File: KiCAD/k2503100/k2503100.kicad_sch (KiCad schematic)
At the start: 14 parts, among them J1 Power, J10 Analog, J11 Digital, J12 PWM, J13 PWM, J14 Communication, J2 PWM, J3 Analog, J4 PWM, J5 Analog, J6 Communication, J7 Digital, J8 Power, J9 Analog

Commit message: 途中
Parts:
- added J15: Power, Connector_PinSocket_2.54mm:PinSocket_1x08_P2.54mm_Vertical, symbol Connector_Generic:Conn_01x08
- added J16, J17: Analog, Connector_PinSocket_2.54mm:PinSocket_1x08_P2.54mm_Vertical, symbol Connector_Generic:Conn_01x08
- added J18: Digital, Connector_PinSocket_2.54mm:PinSocket_2x18_P2.54mm_Vertical, symbol Connector_Generic:Conn_02x18_Odd_Even
- added J19: PWM, Connector_PinSocket_2.54mm:PinSocket_1x10_P2.54mm_Vertical, symbol Connector_Generic:Conn_01x10
- added J20: PWM, Connector_PinSocket_2.54mm:PinSocket_1x08_P2.54mm_Vertical, symbol Connector_Generic:Conn_01x08
- added J21: Communication, Connector_PinSocket_2.54mm:PinSocket_1x08_P2.54mm_Vertical, symbol Connector_Generic:Conn_01x08
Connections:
- net *10: now also J19.8 (Pin_8)
- net *11: now also J19.7 (Pin_7)
- net *12: now also J19.6 (Pin_6)
- net *13: now also J19.5 (Pin_5)
- net *2: now also J20.6 (Pin_6)
- net *3: now also J20.5 (Pin_5)
- net *4: now also J20.4 (Pin_4)
- net *44: now also J18.11 (Pin_11)
- net *45: now also J18.12 (Pin_12)
- net *46: now also J18.9 (Pin_9)
- net *5: now also J20.3 (Pin_3)
- net *52: now also J18.3 (Pin_3)
- net *6: now also J20.2 (Pin_2)
- net *7: now also J20.1 (Pin_1)
- net *8: now also J19.10 (Pin_10)
- net *9: now also J19.9 (Pin_9)
- net +3V3: now also J15.4 (Pin_4)
- net +5V: now also J15.5 (Pin_5), J18.35 (Pin_35), J18.36 (Pin_36)
- net 22: now also J18.33 (Pin_33)
- net 23: now also J18.34 (Pin_34)
- net 24: now also J18.31 (Pin_31)
- net 25: now also J18.32 (Pin_32)
- net 26: now also J18.29 (Pin_29)
- net 27: now also J18.30 (Pin_30)
- net 28: now also J18.27 (Pin_27)
- net 29: now also J18.28 (Pin_28)
- net 30: now also J18.25 (Pin_25)
- net 31: now also J18.26 (Pin_26)
- net 32: now also J18.23 (Pin_23)
- net 33: now also J18.24 (Pin_24)
- net 34: now also J18.21 (Pin_21)
- net 35: now also J18.22 (Pin_22)
- net 36: now also J18.19 (Pin_19)
- net 37: now also J18.20 (Pin_20)
- net 38: now also J18.17 (Pin_17)
- net 39: now also J18.18 (Pin_18)
- net 40: now also J18.15 (Pin_15)
- net 41: now also J18.16 (Pin_16)
- net 42: now also J18.13 (Pin_13)
- net 43: now also J18.14 (Pin_14)
- net 47: now also J18.10 (Pin_10)
- net 48: now also J18.7 (Pin_7)
- net 49: now also J18.8 (Pin_8)
- net 50: now also J18.5 (Pin_5)
- net 51: now also J18.6 (Pin_6)
- net 53: now also J18.4 (Pin_4)
- net A0: now also J16.1 (Pin_1)
- net A1: now also J16.2 (Pin_2)
- net A10: now also J17.3 (Pin_3)
- net A11: now also J17.4 (Pin_4)
- net A12: now also J17.5 (Pin_5)
- net A13: now also J17.6 (Pin_6)
- net A14: now also J17.7 (Pin_7)
- net A15: now also J17.8 (Pin_8)
- net A2: now also J16.3 (Pin_3)
- net A3: now also J16.4 (Pin_4)
- net A4: now also J16.5 (Pin_5)
- net A5: now also J16.6 (Pin_6)
- net A6: now also J16.7 (Pin_7)
- net A7: now also J16.8 (Pin_8)
- net A8: now also J17.1 (Pin_1)
- net A9: now also J17.2 (Pin_2)
- net AREF: now also J19.3 (Pin_3)
- net GND: now also J15.6 (Pin_6), J15.7 (Pin_7), J18.1 (Pin_1), J18.2 (Pin_2), J19.4 (Pin_4)
- net IOREF: now also J15.2 (Pin_2)
- net RX0/0: now also J20.8 (Pin_8)
- net RX1/19: now also J21.6 (Pin_6)
- net RX2/17: now also J21.4 (Pin_4)
- net RX3/15: now also J21.2 (Pin_2)
- net SCL/21: now also J19.1 (Pin_1), J21.8 (Pin_8)
- net SDA/20: now also J19.2 (Pin_2), J21.7 (Pin_7)
- net TX0/1: now also J20.7 (Pin_7)
- net TX1/18: now also J21.5 (Pin_5)
- net TX2/16: now also J21.3 (Pin_3)
- net TX3/14: now also J21.1 (Pin_1)
- net VCC: now also J15.8 (Pin_8)
- net ~{RESET}: now also J15.3 (Pin_3)
- no-connect marks 2 -> 3
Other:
- added sheet Keyboard_Unit (Keyboard.kicad_sch)
- added sheet Relay_UNiT Sheet (Relay_Unit.kicad_sch)
- moved on the sheet: J1, J10, J11, J12, J13, J14, J2, J3, J4, J5, J6, J7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

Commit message: Keyboard_UNiT記述中
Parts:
- removed J1: Power, Connector_PinSocket_2.54mm:PinSocket_1x08_P2.54mm_Vertical, symbol Connector_Generic:Conn_01x08
- removed J2: PWM, Connector_PinSocket_2.54mm:PinSocket_1x10_P2.54mm_Vertical, symbol Connector_Generic:Conn_01x10
- removed J3, J5: Analog, Connector_PinSocket_2.54mm:PinSocket_1x08_P2.54mm_Vertical, symbol Connector_Generic:Conn_01x08
- removed J4: PWM, Connector_PinSocket_2.54mm:PinSocket_1x08_P2.54mm_Vertical, symbol Connector_Generic:Conn_01x08
- removed J6: Communication, Connector_PinSocket_2.54mm:PinSocket_1x08_P2.54mm_Vertical, symbol Connector_Generic:Conn_01x08
- removed J7: Digital, Connector_PinSocket_2.54mm:PinSocket_2x18_P2.54mm_Vertical, symbol Connector_Generic:Conn_02x18_Odd_Even
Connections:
- no-connect marks 3 -> 2
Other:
- sheet Keyboard_Unit renamed Keyboard_UNiT
- sheet Relay_UNiT Sheet renamed Relay_UNiT
- sheet Keyboard_UNiT: file Keyboard.kicad_sch -> Keyboard_UNiT.kicad_sch
- sheet Keyboard_UNiT ports: added +5V, GND, SCL, SDA; removed none
- sheet Relay_UNiT: file Relay_Unit.kicad_sch -> Relay_UNiT.kicad_sch

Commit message: 途中 Relay Unit
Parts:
- removed J10, J9: Analog, Connector_PinSocket_2.54mm:PinSocket_1x08_P2.54mm_Vertical, symbol Connector_Generic:Conn_01x08
- removed J11: Digital, Connector_PinSocket_2.54mm:PinSocket_2x18_P2.54mm_Vertical, symbol Connector_Generic:Conn_02x18_Odd_Even
- removed J12: PWM, Connector_PinSocket_2.54mm:PinSocket_1x10_P2.54mm_Vertical, symbol Connector_Generic:Conn_01x10
- removed J13: PWM, Connector_PinSocket_2.54mm:PinSocket_1x08_P2.54mm_Vertical, symbol Connector_Generic:Conn_01x08
- removed J14: Communication, Connector_PinSocket_2.54mm:PinSocket_1x08_P2.54mm_Vertical, symbol Connector_Generic:Conn_01x08
- removed J8: Power, Connector_PinSocket_2.54mm:PinSocket_1x08_P2.54mm_Vertical, symbol Connector_Generic:Conn_01x08
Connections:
- no-connect marks 2 -> 1
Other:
- sheet Keyboard_UNiT ports: added ~{RESET}; removed none
- sheet Relay_UNiT ports: added +5V, GND, SCL, SDA, ~{RESET}; removed none

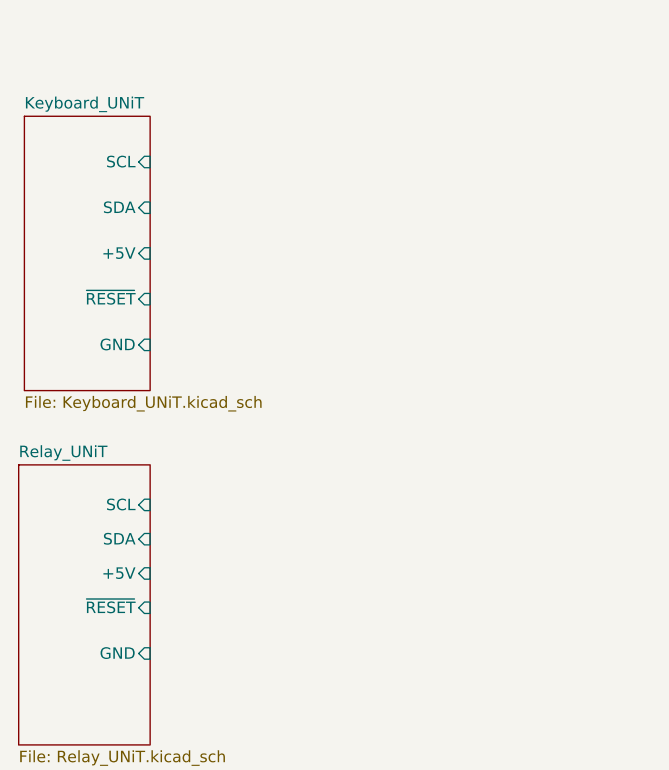
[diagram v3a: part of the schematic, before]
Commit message: Relay_UNiTの端子名入れ途中
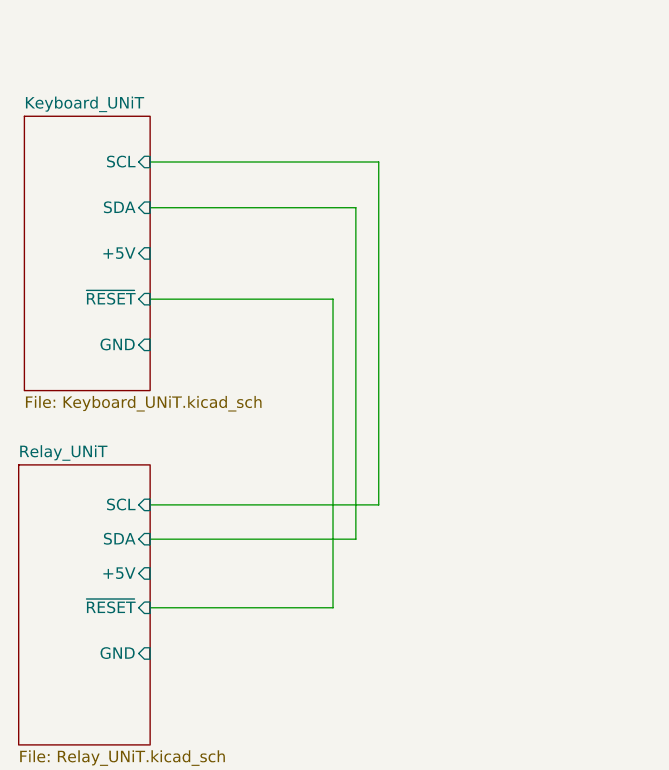
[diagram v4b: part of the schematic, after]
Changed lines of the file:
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@@
     (stroke (width 0) (type solid))
+  )
+  (wire (pts (xy 97.79 68.58) (xy 97.79 106.68))
+    (stroke (width 0) (type default))
   )
   (wire (pts (xy 257.175 88.265) (xy 269.875 88.265))
@@
     (stroke (width 0) (type solid))
   )
+  (wire (pts (xy 72.39 73.66) (xy 95.25 73.66))
+    (stroke (width 0) (type default))
+  )
   (wire (pts (xy 257.175 47.625) (xy 269.875 47.625))
     (stroke (width 0) (type solid))
@@
     (stroke (width 0) (type solid))
   )
+  (wire (pts (xy 92.71 118.11) (xy 72.39 118.11))
+    (stroke (width 0) (type default))
+  )
   (wire (pts (xy 257.175 67.945) (xy 269.875 67.945))
     (stroke (width 0) (type solid))
@@
     (stroke (width 0) (type solid))
   )
+  (wire (pts (xy 95.25 73.66) (xy 95.25 110.49))
+    (stroke (width 0) (type default))
+  )
   (wire (pts (xy 233.68 121.285) (xy 233.68 131.445))
     (stroke (width 0) (type solid))
@@
     (stroke (width 0) (type solid))
   )
+  (wire (pts (xy 72.39 68.58) (xy 97.79 68.58))
+    (stroke (width 0) (type default))
+  )
   (wire (pts (xy 216.535 62.865) (xy 229.235 62.865))
     (stroke (width 0) (type solid))
@@
     (stroke (width 0) (type solid))
   )
+  (wire (pts (xy 72.39 83.82) (xy 92.71 83.82))
+    (stroke (width 0) (type default))
+  )
   (wire (pts (xy 257.175 98.425) (xy 269.875 98.425))
     (stroke (width 0) (type solid))
   )
+  (wire (pts (xy 95.25 110.49) (xy 72.39 110.49))
+    (stroke (width 0) (type default))
+  )
   (wire (pts (xy 236.22 121.285) (xy 236.22 131.445))
     (stroke (width 0) (type solid))
@@
     (stroke (width 0) (type solid))
   )
+  (wire (pts (xy 92.71 83.82) (xy 92.71 118.11))
+    (stroke (width 0) (type default))
+  )
   (wire (pts (xy 226.06 144.145) (xy 226.06 154.305))
     (stroke (width 0) (type solid))
@@
     (stroke (width 0) (type solid))
   )
+  (wire (pts (xy 97.79 106.68) (xy 72.39 106.68))
+    (stroke (width 0) (type default))
+  )
   (wire (pts (xy 213.995 34.925) (xy 229.235 34.925))

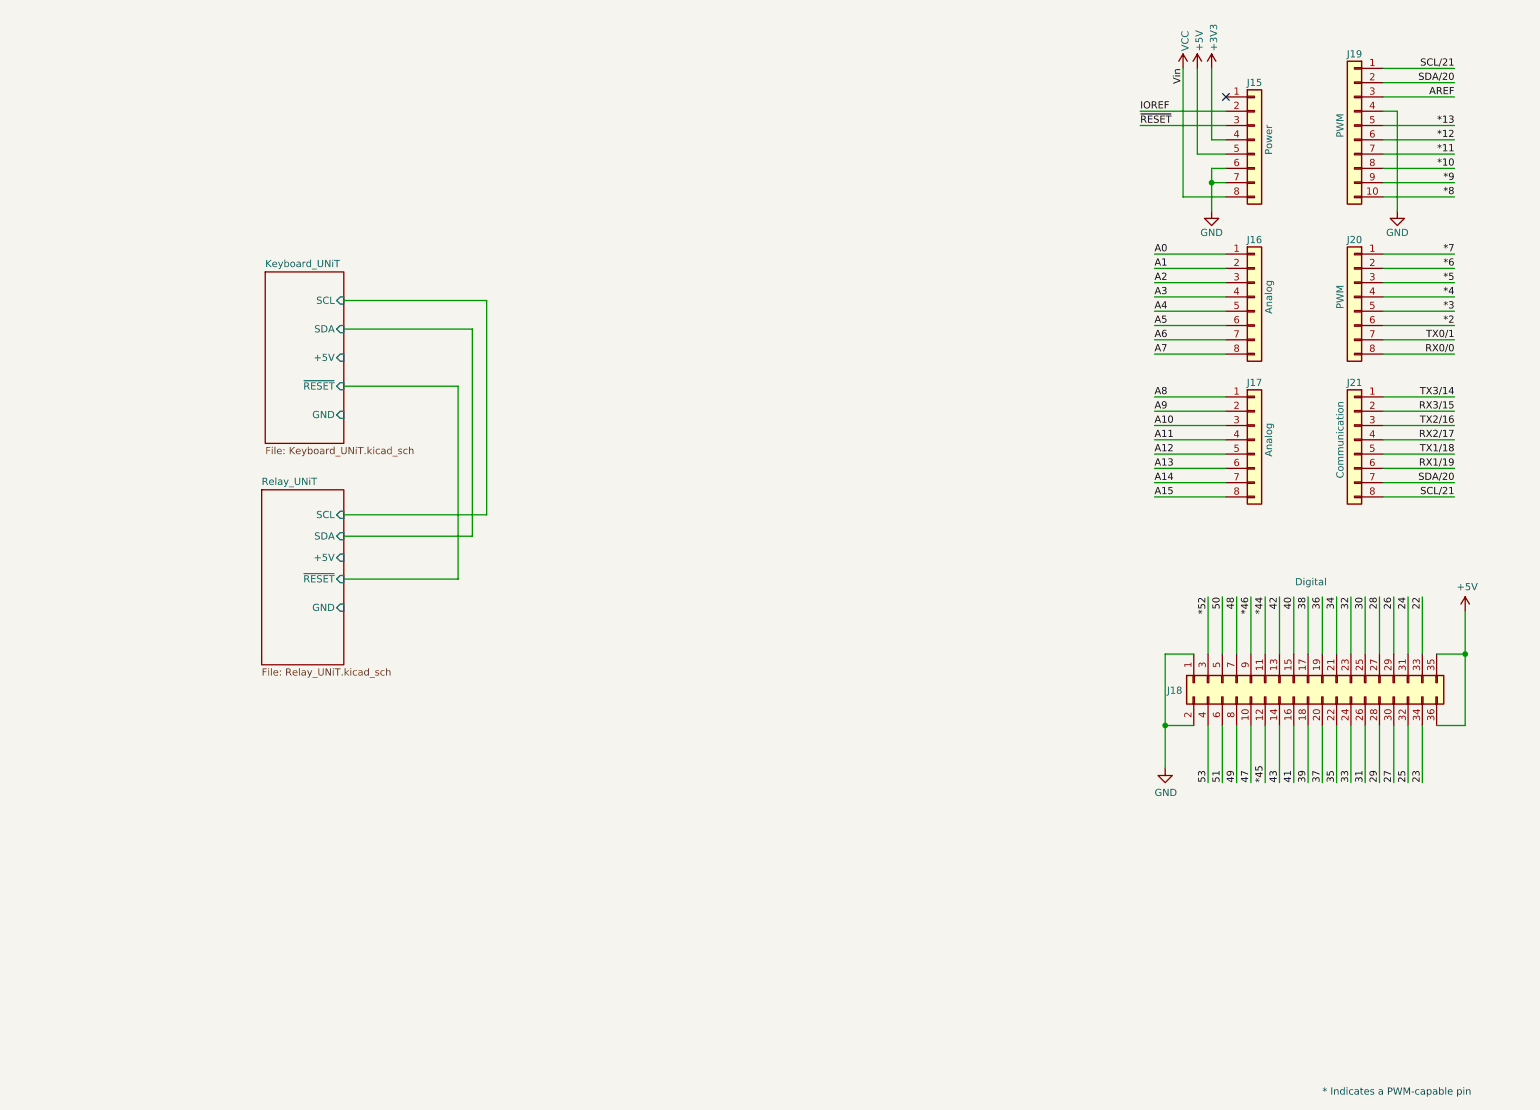
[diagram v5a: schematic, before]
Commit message: MP86A1のパーツ作成
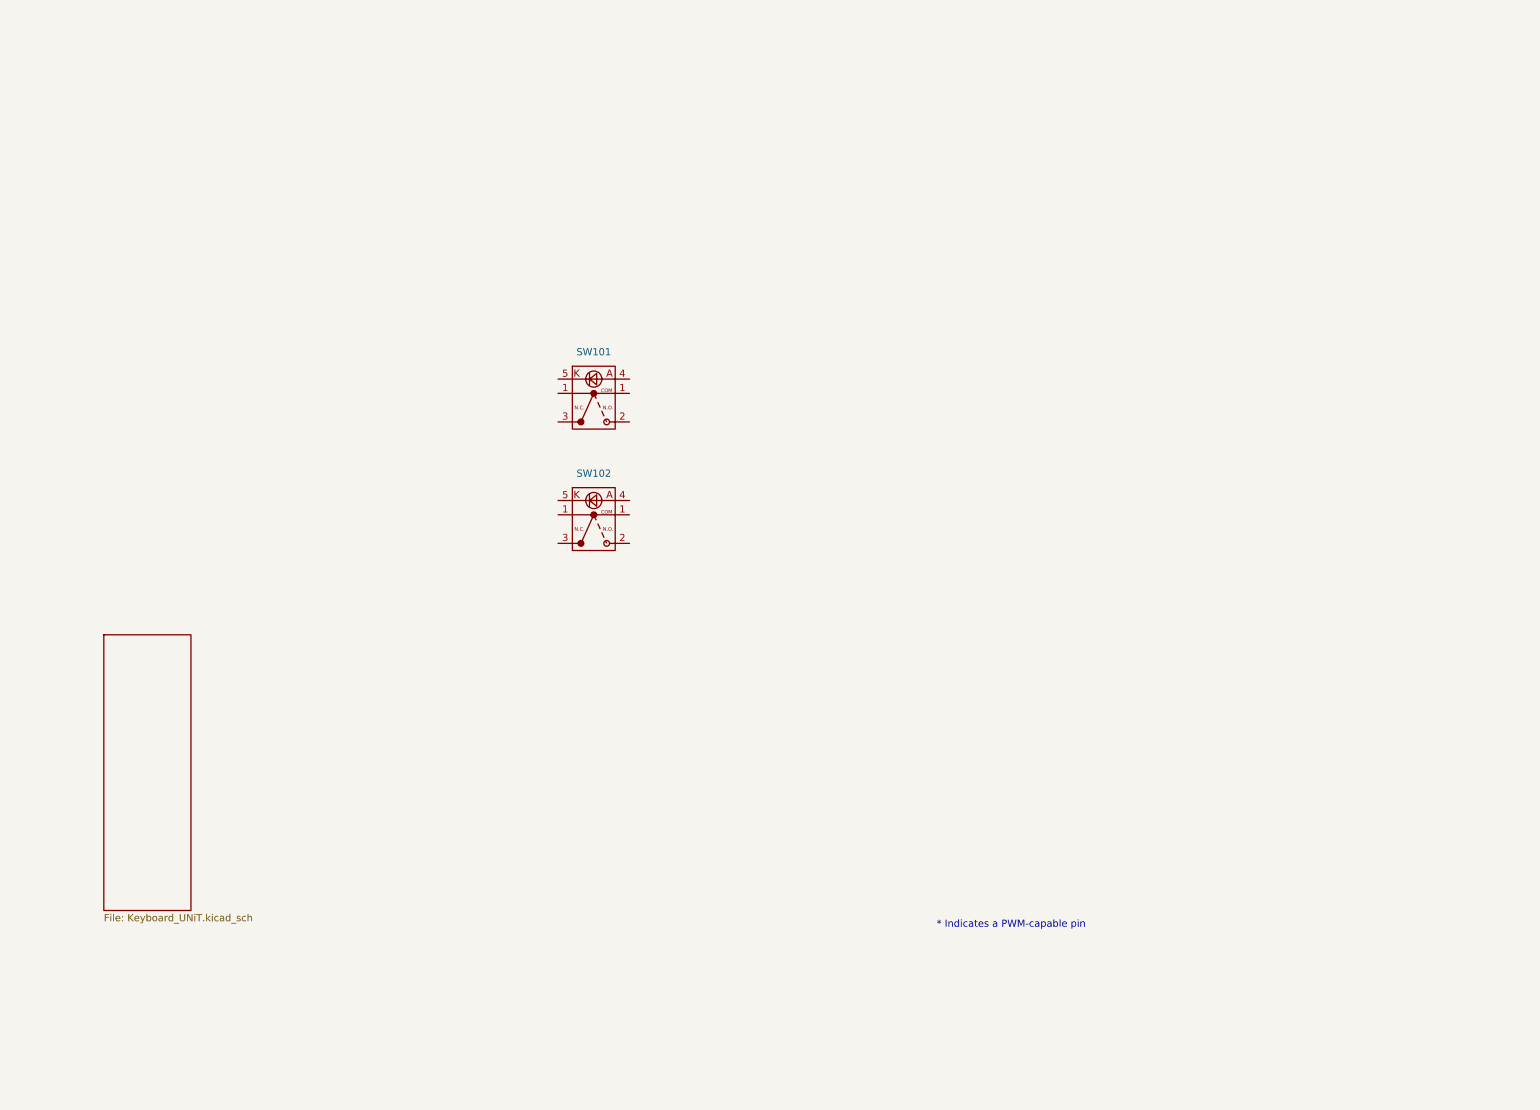
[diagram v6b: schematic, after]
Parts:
- removed J15: Power, Connector_PinSocket_2.54mm:PinSocket_1x08_P2.54mm_Vertical, symbol Connector_Generic:Conn_01x08
- removed J16, J17: Analog, Connector_PinSocket_2.54mm:PinSocket_1x08_P2.54mm_Vertical, symbol Connector_Generic:Conn_01x08
- removed J18: Digital, Connector_PinSocket_2.54mm:PinSocket_2x18_P2.54mm_Vertical, symbol Connector_Generic:Conn_02x18_Odd_Even
- removed J19: PWM, Connector_PinSocket_2.54mm:PinSocket_1x10_P2.54mm_Vertical, symbol Connector_Generic:Conn_01x10
- removed J20: PWM, Connector_PinSocket_2.54mm:PinSocket_1x08_P2.54mm_Vertical, symbol Connector_Generic:Conn_01x08
- removed J21: Communication, Connector_PinSocket_2.54mm:PinSocket_1x08_P2.54mm_Vertical, symbol Connector_Generic:Conn_01x08
- added SW101: ~, symbol K2503100:MP86A1
- added SW102: ~, HOLLY2:MP86A1, symbol K2503100:MP86A1
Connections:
- no-connect marks 1 -> 0
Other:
- removed sheet Relay_UNiT
- sheet Keyboard_UNiT ports: added none; removed +5V, GND, SCL, SDA, ~{RESET}

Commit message: KYBD_UNit途中
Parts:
- removed SW101: ~, symbol K2503100:MP86A1
- removed SW102: ~, HOLLY2:MP86A1, symbol K2503100:MP86A1
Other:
- added sheet KYBD_UNiT (KYBD_UNit.kicad_sch)
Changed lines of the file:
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@@
-		)
-	)
-	(symbol
-		(lib_name "K2503100:MP86A1")
-		(lib_id "K2503100:MP86A1")
-		(at 116.84 100.33 0)
-		(unit 1)
-		(exclude_from_sim no)
-		(in_bom yes)
-		(on_board yes)
-		(dnp no)
-		(fields_autoplaced yes)
-		(property "Reference" "SW102"
-			(at 116.84 99.3225 0)
-			(effects
-				(font
-					(size 1.27 1.27)
-				)
-			)
-		)
-		(property "Value" "~"
-			(at 116.84 101.0039 0)
-			(effects
-				(font
-					(size 1.27 1.27)
-				)
-			)
-		)
-		(property "Footprint" "HOLLY2:MP86A1"
-			(at 116.84 100.33 0)
-			(effects
-				(font
-					(size 1.27 1.27)
-				)
-				(hide yes)
-			)
-		)
-		(property "Datasheet" ""
-			(at 116.84 100.33 0)
-			(effects
-				(font
-					(size 1.27 1.27)
-				)
-				(hide yes)
-			)
-		)
-		(property "Description" ""
-			(at 116.84 100.33 0)
-			(effects
-				(font
-					(size 1.27 1.27)
-				)
-				(hide yes)
-			)
-		)
-		(pin "3"
-		)
-		(pin "1"
-		)
-		(pin "5"
-		)
-		(pin "2"
-		)
-		(pin "4"
-		)
-		(pin "1"
-		)
-		(instances
-			(project ""
-				(path "/e63e39d7-6ac0-4ffd-8aa3-1841a4541b55"
-					(reference "SW102")
-					(unit 1)
-				)
-			)
-		)
-	)
-	(symbol
-		(lib_id "K2503100:MP86A1")
-		(at 116.84 78.74 0)
-		(unit 1)
-		(exclude_from_sim no)
-		(in_bom yes)
-		(on_board yes)
-		(dnp no)
-		(fields_autoplaced yes)
-		(property "Reference" "SW101"
-			(at 116.84 77.7325 0)
-			(effects
-				(font
-					(size 1.27 1.27)
-				)
-			)
-		)
-		(property "Value" "~"
-			(at 116.84 79.4139 0)
-			(effects
-				(font
-					(size 1.27 1.27)
-				)
-			)
-		)
-		(property "Footprint" ""
-			(at 116.84 78.74 0)
-			(effects
-				(font
-					(size 1.27 1.27)
-				)
-				(hide yes)
-			)
-		)
-		(property "Datasheet" ""
-			(at 116.84 78.74 0)
-			(effects
-				(font
-					(size 1.27 1.27)
-				)
-				(hide yes)
-			)
-		)
-		(property "Description" ""
-			(at 116.84 78.74 0)
-			(effects
-				(font
-					(size 1.27 1.27)
-				)
-				(hide yes)
-			)
-		)
-		(pin "3"
-		)
-		(pin "1"
-		)
-		(pin "5"
-		)
-		(pin "2"
-		)
-		(pin "4"
-		)
-		(pin "1"
-		)
-		(instances
-			(project ""
-				(path "/e63e39d7-6ac0-4ffd-8aa3-1841a4541b55"
-					(reference "SW101")
-					(unit 1)
-				)
-			)
 		)
 	)
@@
 				)
 			)
+		)
+	)
+	(sheet
+		(at 38.1 57.15)
+		(size 12.7 20.32)
+		(fields_autoplaced yes)
+		(stroke
+			(width 0.1524)
+			(type solid)
+		)
+		(fill
+			(color 0 0 0 0.0000)
+		)
+		(property "Sheetname" "KYBD_UNiT"
+			(at 38.1 56.4384 0)
+			(effects
+				(font
+					(size 1.27 1.27)
+				)
+				(justify left bottom)
+			)
+		)
+		(property "Sheetfile" "KYBD_UNit.kicad_sch"
+			(at 38.1 78.0546 0)
+			(effects
+				(font
+					(size 1.27 1.27)
+				)
+				(justify left top)
+			)
+		)
+		(instances
+			(project "k2503100"
+				(path "/e63e39d7-6ac0-4ffd-8aa3-1841a4541b55"
+					(page "3")
+				)
+			)
